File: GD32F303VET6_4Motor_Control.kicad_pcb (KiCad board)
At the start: 6 copper layers, 100 x 60 mm, 156 parts, among them CN1 KF2EDGK-5.08-2P, CN4 WJ15EDGRC-3.81-2P, CN5 KF15EDGRC3.81-6P, CN6 KF15EDGRC3.81-6P, CN7 KF15EDGRC3.81-6P, CN8 KF15EDGRC3.81-6P, J1 TYPE-C-31-M-31, J2 TYPE-C 16PIN 2MD(073), Q16 CJ3134K KF, Q17 CJ3134K KF, Q3 CJ3134K, SW1 SKRPACE010, U1 XL1509-5.0, U13 SIT3485ESA, U15 TXS0104EPWR, U19 CH340N, U20 LM66100DCKR, U21 LM66100DCKR, U22 SN74LVC2G06DBVR, U23 SN74LVC2G06DBVR, U24 SN74LVC2G06DBVR, U25 SN74LVC2G06DBVR, U5 LM66100DCKR, U6 SY8089A1AAC, U7 GD32F303VET6, U8 GD25Q16ESIGR, Y1 TAXM8M4RDBCCT2T, Y2 XKXGI-SUA-32.768K

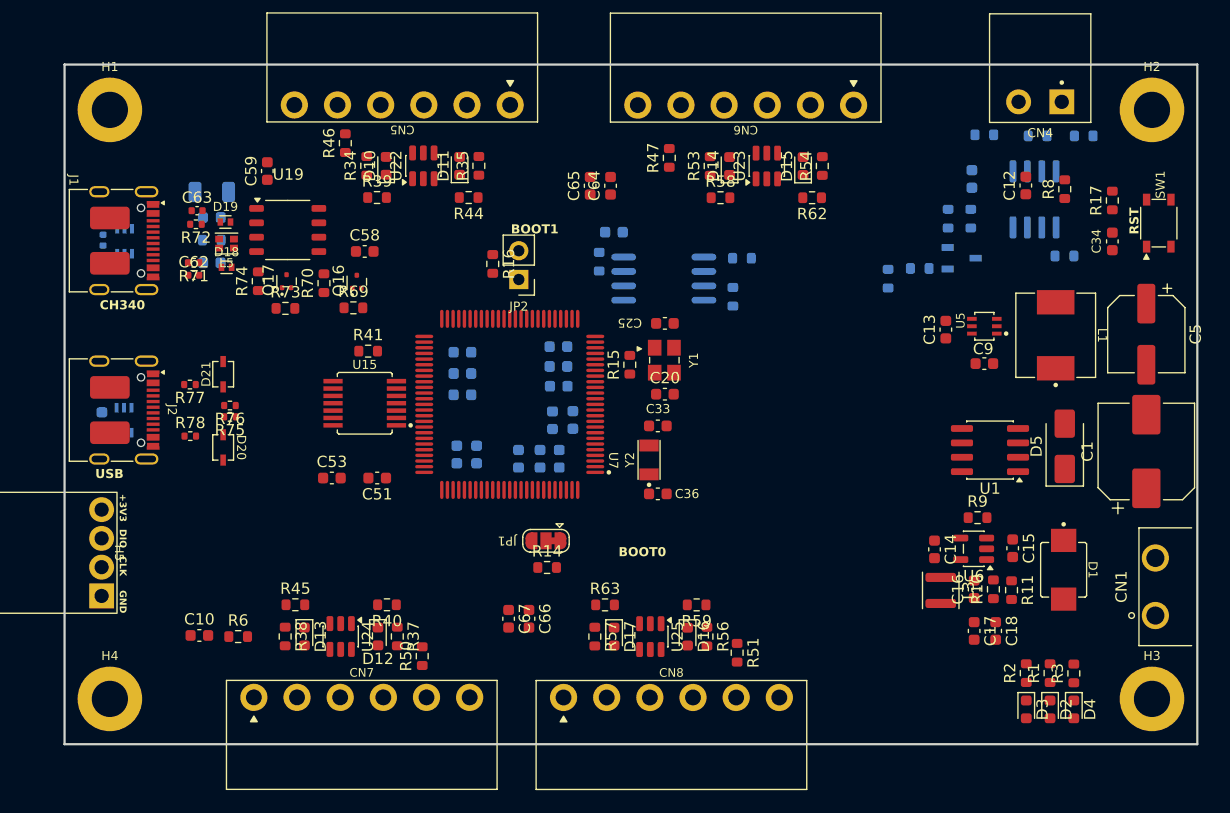
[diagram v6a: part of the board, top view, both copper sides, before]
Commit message: 优化 MCU 符号与通道命名并同步 V2.0 PCB
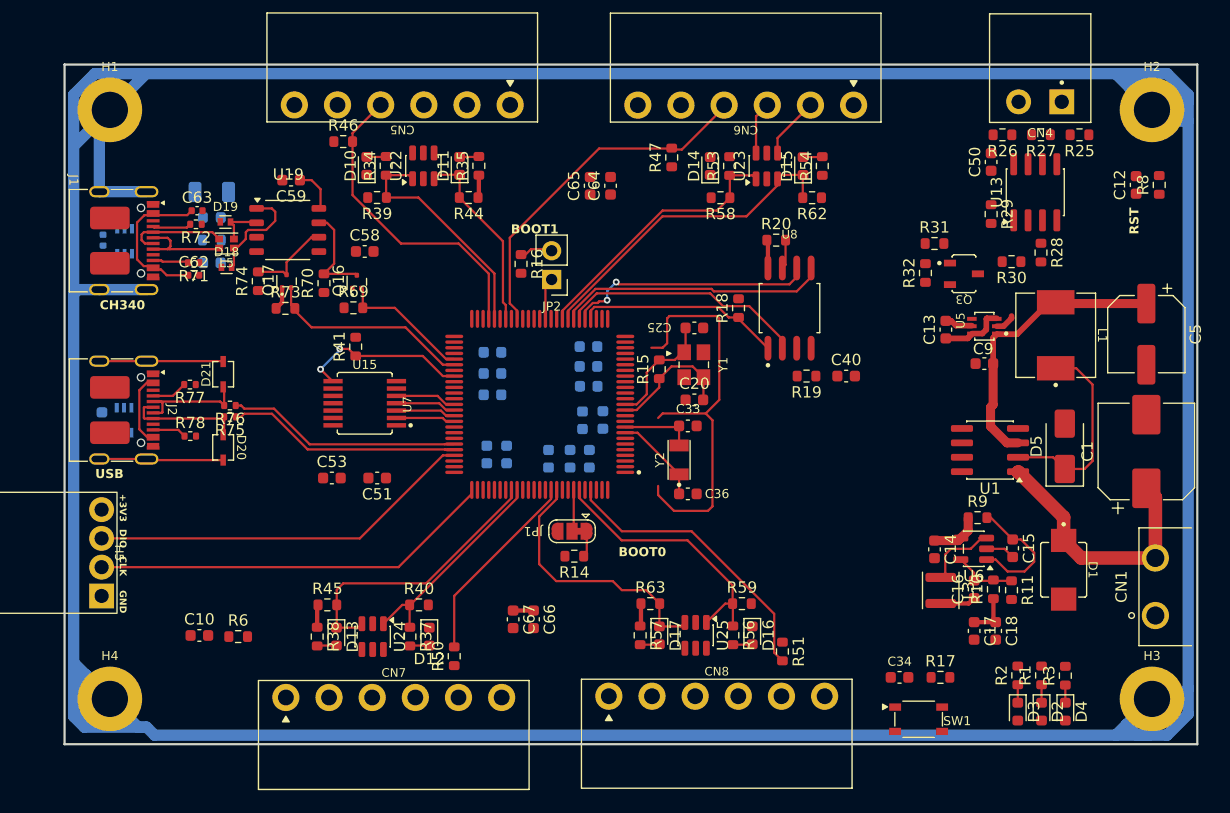
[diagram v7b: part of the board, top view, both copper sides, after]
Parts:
- C40, C50, Q3, R18, R19, R20, R25, R26, R27, R28, R29, R30, R31, R32, U13, U8: moved to F.Cu
- moved SW1 48.7 mm to (160.9, 116.8), turned to 0 degrees
- moved R17 44.8 mm to (162.8, 113.1), turned to 0 degrees
- moved C39 42.8 mm to (159.2, 113.1), turned to 180 degrees
- moved C40 24.1 mm to (154.5, 86.5)
- moved R20 15.7 mm to (148.3, 74.5), turned to 0 degrees
- moved U8 11.4 mm to (149.5, 80.5), turned to 0 degrees
- moved C12 9.74 mm to (180.1, 69.6)
- moved R19 9.55 mm to (151.0, 86.5), turned to 180 degrees
- moved R25 8.40 mm to (175.1, 65.2), turned to 180 degrees
- moved R8 8.35 mm to (182.1, 69.6)
- moved R29 7.46 mm to (167.3, 72.2), turned to -90 degrees
- moved R26 7.18 mm to (168.3, 65.2), turned to 180 degrees
- moved R28 6.89 mm to (171.7, 75.6)
- moved R30 6.77 mm to (169.1, 76.4), turned to 180 degrees
- moved D16 5.71 mm to (146.2, 109.4)
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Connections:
- net /MCU_Core/BRAKE1_1 renamed /MCU_Core/BRAKE1
- net /MCU_Core/BRAKE1_2 renamed /MCU_Core/BRAKE2
- net /MCU_Core/BRAKE1_3 renamed /MCU_Core/BRAKE3
- net /MCU_Core/BRAKE1_4 renamed /MCU_Core/BRAKE4
- net /MCU_Core/CAN_RX renamed /CAN/CAN_RXD
- net /MCU_Core/CAN_TX renamed /CAN/CAN_TXD
- net /MCU_Core/DIR1_1 renamed /MCU_Core/DIR1
- net /MCU_Core/DIR1_2 renamed /MCU_Core/DIR2
- net /MCU_Core/DIR1_3 renamed /MCU_Core/DIR3
- net /MCU_Core/DIR1_4 renamed /MCU_Core/DIR4
- net /MCU_Core/FG1_1 renamed /MCU_Core/FG1
- net /MCU_Core/FG1_2 renamed /MCU_Core/FG2
- net /MCU_Core/FG1_3 renamed /MCU_Core/FG3
- net /MCU_Core/Motor_Comm/MOTOR_BRAKE1_1 renamed /MCU_Core/Motor_Comm/MOTOR_BRAKE1
- net /MCU_Core/Motor_Comm/MOTOR_BRAKE1_2 renamed /MCU_Core/Motor_Comm/MOTOR_BRAKE2
- net /MCU_Core/Motor_Comm/MOTOR_BRAKE1_3 renamed /MCU_Core/Motor_Comm/MOTOR_BRAKE3
- net /MCU_Core/Motor_Comm/MOTOR_BRAKE1_4 renamed /MCU_Core/Motor_Comm/MOTOR_BRAKE4
- net /MCU_Core/Motor_Comm/MOTOR_DIR1_1 renamed /MCU_Core/Motor_Comm/MOTOR_DIR1
- net /MCU_Core/Motor_Comm/MOTOR_DIR1_2 renamed /MCU_Core/Motor_Comm/MOTOR_DIR2
- net /MCU_Core/Motor_Comm/MOTOR_DIR1_3 renamed /MCU_Core/Motor_Comm/MOTOR_DIR3
- net /MCU_Core/Motor_Comm/MOTOR_DIR1_4 renamed /MCU_Core/Motor_Comm/MOTOR_DIR4
- net /MCU_Core/Motor_Comm/PWM1_5V_1 renamed /MCU_Core/Motor_Comm/PWM_5V1
- net /MCU_Core/Motor_Comm/PWM1_5V_2 renamed /MCU_Core/Motor_Comm/PWM_5V2
- net /MCU_Core/Motor_Comm/PWM1_5V_3 renamed /MCU_Core/Motor_Comm/PWM_5V3
- net /MCU_Core/Motor_Comm/PWM1_5V_4 renamed /MCU_Core/Motor_Comm/PWM_5V4
- net /MCU_Core/RS485_RX renamed /RS485/RS485_RX
- net /MCU_Core/RS485_TX renamed /RS485/RS485_TX
- CN8 pad 4: /MCU_Core/FG1_4 -> /MCU_Core/FG4
- R51 pad 2: /MCU_Core/FG1_4 -> /MCU_Core/FG4
- U15 pad 2: /MCU_Core/PWM1_4 -> /MCU_Core/PWM4
- U15 pad 3: /MCU_Core/PWM1_3 -> /MCU_Core/PWM3
- U15 pad 4: /MCU_Core/PWM1_2 -> /MCU_Core/PWM2
- U15 pad 5: /MCU_Core/PWM1_1 -> /MCU_Core/PWM1
- U7 pad 23: /MCU_Core/FG1_4 -> unconnected-(U7C-PA0-Pad23)
- U7 pad 55: /MCU_Core/WIFI_TX -> /MCU_Core/USART0_TX
- U7 pad 56: /MCU_Core/WIFI_RX -> /MCU_Core/USART0_RX
- U7 pad 59: /MCU_Core/PWM1_1 -> unconnected-(U7C-PD12-Pad59)
- U7 pad 60: /MCU_Core/PWM1_2 -> unconnected-(U7C-PD13-Pad60)
- U7 pad 61: /MCU_Core/PWM1_3 -> unconnected-(U7C-PD14-Pad61)
- U7 pad 62: /MCU_Core/PWM1_4 -> unconnected-(U7C-PD15-Pad62)
- U7 pad 63: unconnected-(U7E-PC6/I2S1_MCK/TIMER7_CH0/SDIO_D6-Pad63) -> /MCU_Core/PWM1
- U7 pad 64: unconnected-(U7E-PC7/I2S2_MCK/TIMER7_CH1/SDIO_D7-Pad64) -> /MCU_Core/PWM2
- U7 pad 65: unconnected-(U7E-PC8/TIMER7_CH2/SDIO_D0-Pad65) -> /MCU_Core/PWM3
- U7 pad 66: unconnected-(U7E-PC9/TIMER7_CH3/SDIO_D1-Pad66) -> /MCU_Core/PWM4
- U7 pad 68: /MCU_Core/USART0_TX -> /MCU_Core/WIFI_TX
- U7 pad 69: /MCU_Core/USART0_RX -> /MCU_Core/WIFI_RX
- U7 pad 97: unconnected-(U7E-PE0/TIMER3_ETI/EXMC_NBL0-Pad97) -> /MCU_Core/FG4
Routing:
- net Earth: track 0.00 -> 396.6 mm
- net (no net): track 0.00 -> 36.6 mm
- net /MCU_Core/SWCLK: track 0.00 -> 35.7 mm
- net /MCU_Core/SWDIO: track 0.00 -> 34.2 mm
- net /MCU_Core/FG2: track 0.00 -> 31.5 mm
- net /MCU_Core/BRAKE2: track 0.00 -> 28.8 mm
- net /MCU_Core/FG1: track 0.00 -> 27.9 mm
- net BOARD_5V_RAW: track 0.00 -> 25.8 mm
- net /MCU_Core/FG4: track 0.00 -> 25.7 mm
- net /MCU_Core/BRAKE3: track 0.00 -> 25.2 mm
- net /MCU_Core/DIR2: track 0.00 -> 24.6 mm
- net /MCU_Core/DIR4: track 0.00 -> 24.0 mm
- net /MCU_Core/MCU_SPI_MOSI: track 0.00 -> 23.9 mm
- net /MCU_Core/BRAKE4: track 0.00 -> 23.7 mm
- net +24V: track 0.00 -> 22.9 mm
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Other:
- board text added: "BRAKE1"
- board text added: "BRAKE2"
- board text added: "BRAKE3"
- board text added: "BRAKE4"
- board text added: "DIR1"
- board text added: "DIR2"
- board text added: "DIR3"
- board text added: "DIR4"
- board text added: "FG1"
- board text added: "FG2"
- board text added: "FG3"
- board text added: "FG4"
- board text added: "PWM1"
- board text added: "PWM2"
- board text added: "PWM3"
- board text added: "PWM4"
- board text removed: "BRAKE1_1"
- board text removed: "BRAKE1_2"
- board text removed: "BRAKE1_3"
- board text removed: "BRAKE1_4"
- board text removed: "DIR1_1"
- board text removed: "DIR1_2"
- board text removed: "DIR1_3"
- board text removed: "DIR1_4"
- board text removed: "FG1_1"
- board text removed: "FG1_2"
- board text removed: "FG1_3"
- board text removed: "FG1_4"
- board text removed: "PWM1_1"
- board text removed: "PWM1_2"
- board text removed: "PWM1_3"
- board text removed: "PWM1_4"

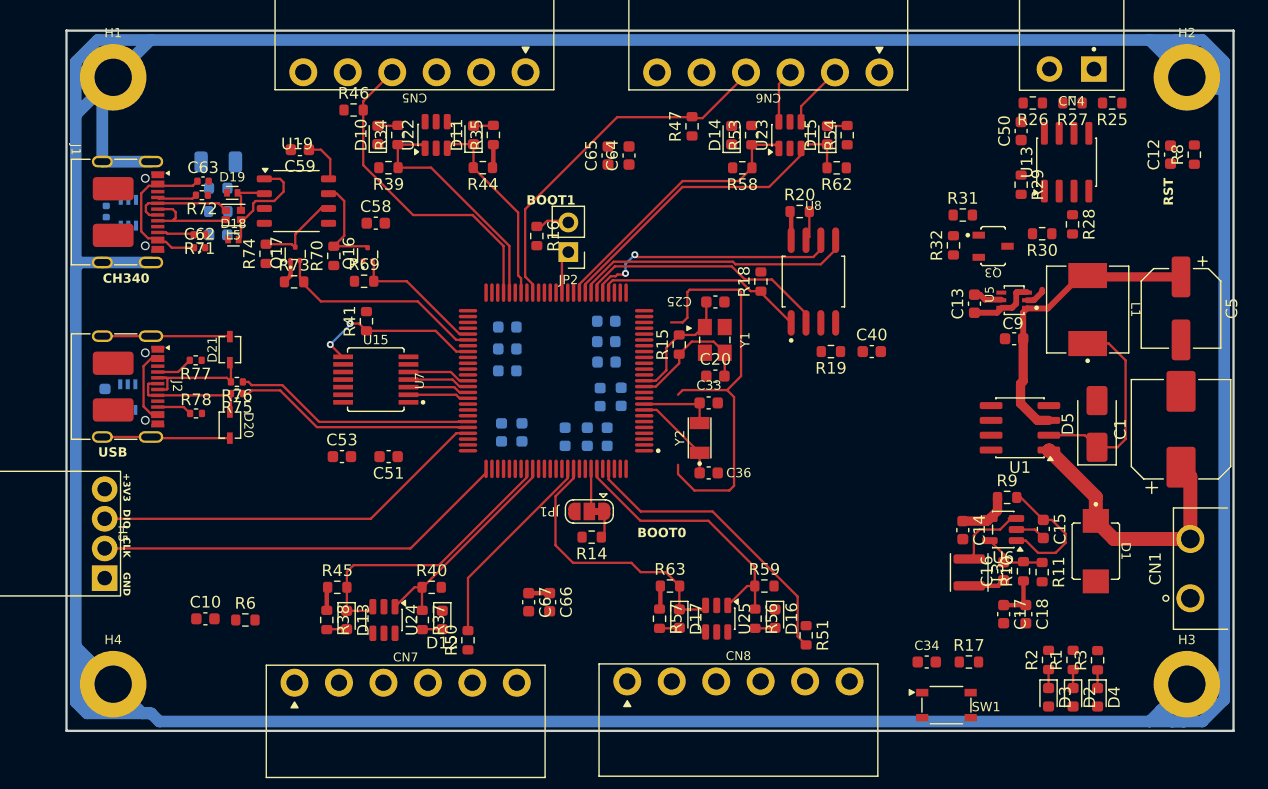
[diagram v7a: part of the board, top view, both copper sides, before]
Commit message: 更新 V2.0 PCB 布局与孔间隙规则
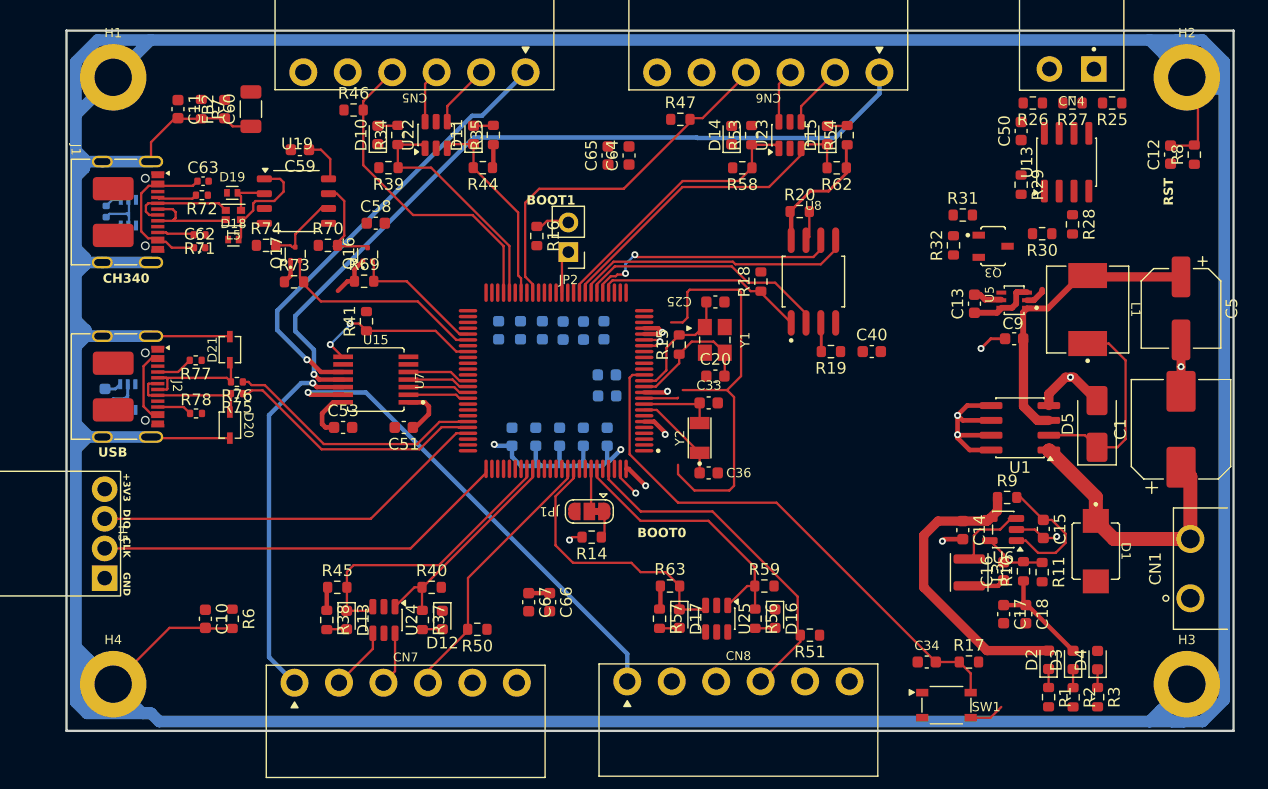
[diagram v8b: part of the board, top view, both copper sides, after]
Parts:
- C11, C60, FB2, R7: moved to F.Cu
- moved C11 11.3 mm to (95.0, 65.7), turned to -90 degrees
- moved R7 8.89 mm to (97.0, 65.7), turned to -90 degrees
- moved FB2 6.80 mm to (99.0, 65.7), turned to 90 degrees
- moved C60 5.32 mm to (101.3, 65.7), turned to 90 degrees
- moved D2 3.84 mm to (169.7, 112.9), turned to 90 degrees
- moved D3 3.83 mm to (171.8, 112.9), turned to 90 degrees
- moved R2 3.83 mm to (171.8, 116.1), turned to -90 degrees
- moved R1 3.82 mm to (169.7, 116.1), turned to -90 degrees
- moved C35 3.79 mm to (128.1, 84.7), turned to -90 degrees
- moved C30 3.56 mm to (122.5, 84.7), turned to -90 degrees
- moved D4 3.19 mm to (173.8, 112.9), turned to 90 degrees
- moved R3 3.16 mm to (173.8, 116.1), turned to -90 degrees
- moved C28 3.01 mm to (126.3, 84.7), turned to -90 degrees
- moved C51 2.82 mm to (114.4, 93.0)
- moved C34 2.73 mm to (131.6, 84.7), turned to -90 degrees
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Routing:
- net /MCU_Core/Motor_Comm/PWM_5V2: track 0.00 -> 68.2 mm, vias 0 -> 1
- net +3V3: track 19.6 -> 73.3 mm, vias 0 -> 6
- net GND: track 6.87 -> 60.4 mm, vias 0 -> 10
- net /MCU_Core/NRST: track 0.00 -> 46.6 mm
- net Earth: track 396.6 -> 440.9 mm
- net /MCU_Core/Motor_Comm/PWM_5V4: track 0.00 -> 42.1 mm, vias 0 -> 1
- net /MCU_Core/Motor_Comm/PWM_5V1: track 0.00 -> 38.5 mm, vias 0 -> 1
- net /MCU_Core/Motor_Comm/PWM_5V3: track 0.00 -> 31.5 mm, vias 0 -> 1
- net +5V: track 10.3 -> 35.8 mm
- net /MCU_Core/FG3: track 17.4 -> 23.3 mm
- net /MCU_Core/Motor_Comm/MOTOR_BRAKE1: track 0.00 -> 5.44 mm
- net /MCU_Core/Motor_Comm/MOTOR_BRAKE3: track 0.00 -> 5.44 mm
- net /MCU_Core/Motor_Comm/MOTOR_DIR1: track 0.00 -> 4.65 mm
- net /MCU_Core/Motor_Comm/MOTOR_DIR3: track 0.00 -> 4.65 mm
- net /MCU_Core/FG4: track 25.7 -> 30.0 mm
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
